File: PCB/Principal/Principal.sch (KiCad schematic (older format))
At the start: 17 parts, among them J1 STM32_P1, J2 STM32_P2, J3 Sensor_Golpes, J4 Teclado, J5 Sensor_Unidades, J6 Display_16x2, J7 Lector_RFID, J8 IN_Alimentación, SW1 SW_Power

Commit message: Alta plaquita guacho
Hay que acomodarla pero no quedo ningun puente.
Cambie TODOS los GPIO. Atento.
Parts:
- removed SW1: SW_Power, symbol Switch:SW_DPST
- added RV1: Display_Brillo, Potentiometers:Potentiometer_Trimmer_Bourns_3266Y, symbol Device:R_POT_TRIM_US
- D1: footprint (none) -> LEDs:LED_D5.0mm
- J1, J2: footprint Pin_Headers:Pin_Header_Straight_2x25_Pitch2.00mm -> Pin_Headers:Pin_Header_Straight_2x25_Pitch2.54mm
- J3, J5, J7: footprint (none) -> Connectors_Terminal_Blocks:TerminalBlock_bornier-3_P5.08mm
- J4: footprint (none) -> Pin_Headers:Pin_Header_Straight_1x08_Pitch2.54mm
- J6: footprint (none) -> Pin_Headers:Pin_Header_Straight_1x16_Pitch2.54mm
- J8: footprint (none) -> Connectors_Terminal_Blocks:TerminalBlock_bornier-2_P5.08mm
- R1, R2, R3, R4, R5, R6, R7: footprint (none) -> Resistors_THT:R_Axial_DIN0207_L6.3mm_D2.5mm_P10.16mm_Horizontal
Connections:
- wire segments 71 -> 104
- no-connect marks 0 -> 90
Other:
- moved on the sheet: D1, J3, J4, J5, J6, J7, J8, R1, R2, R3, R4, R5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

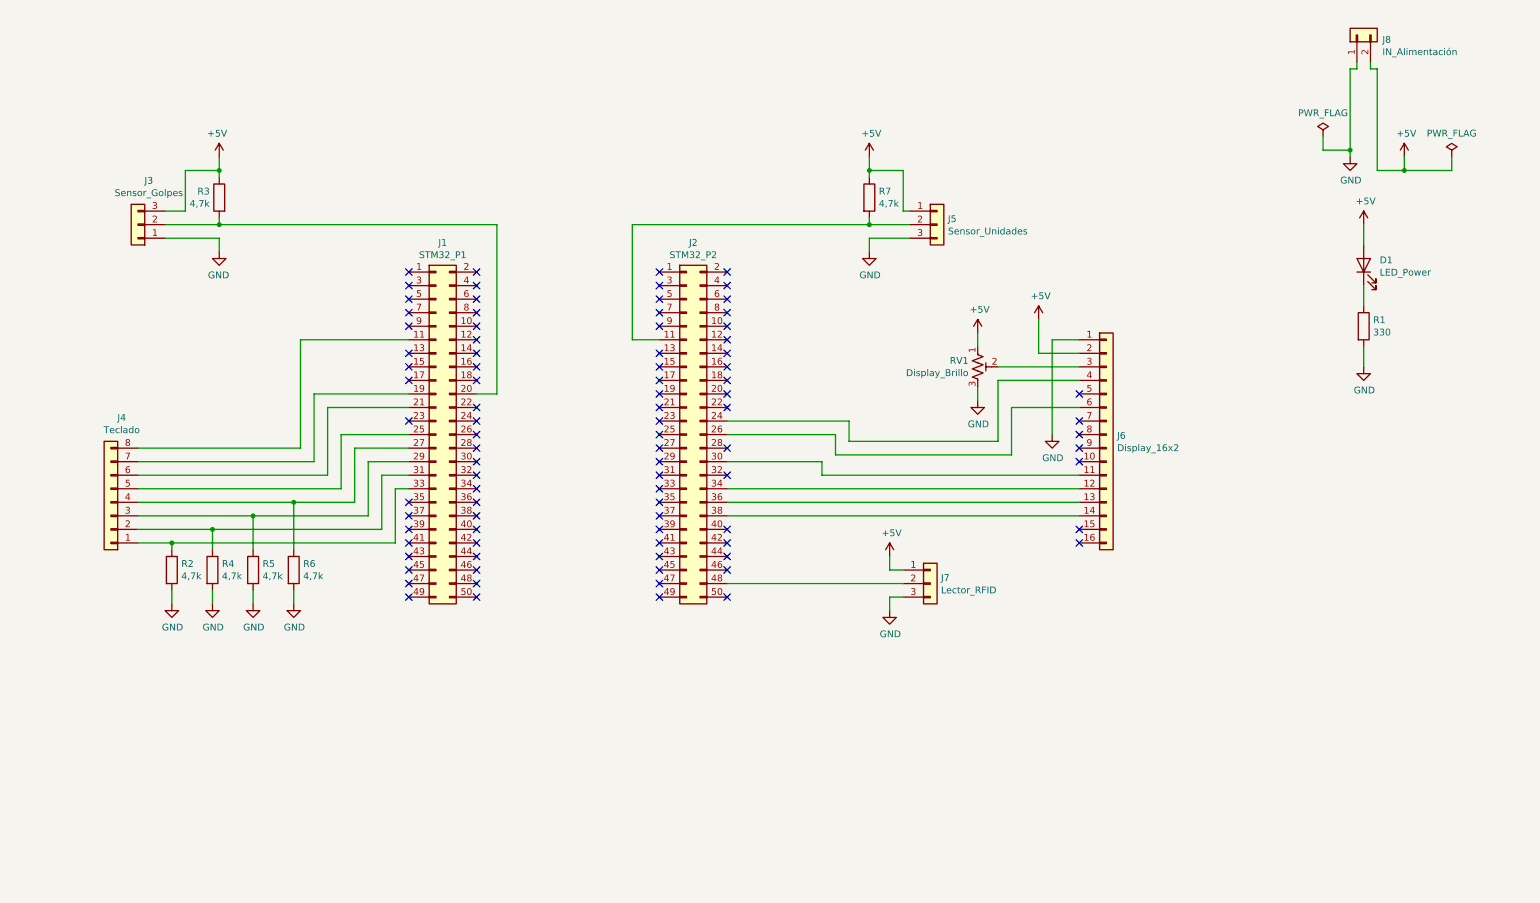
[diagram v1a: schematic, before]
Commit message: Sumando cambios al PCB
Se agrego al esquematico fuente de 5V con 7805 y la conexion del rfid.
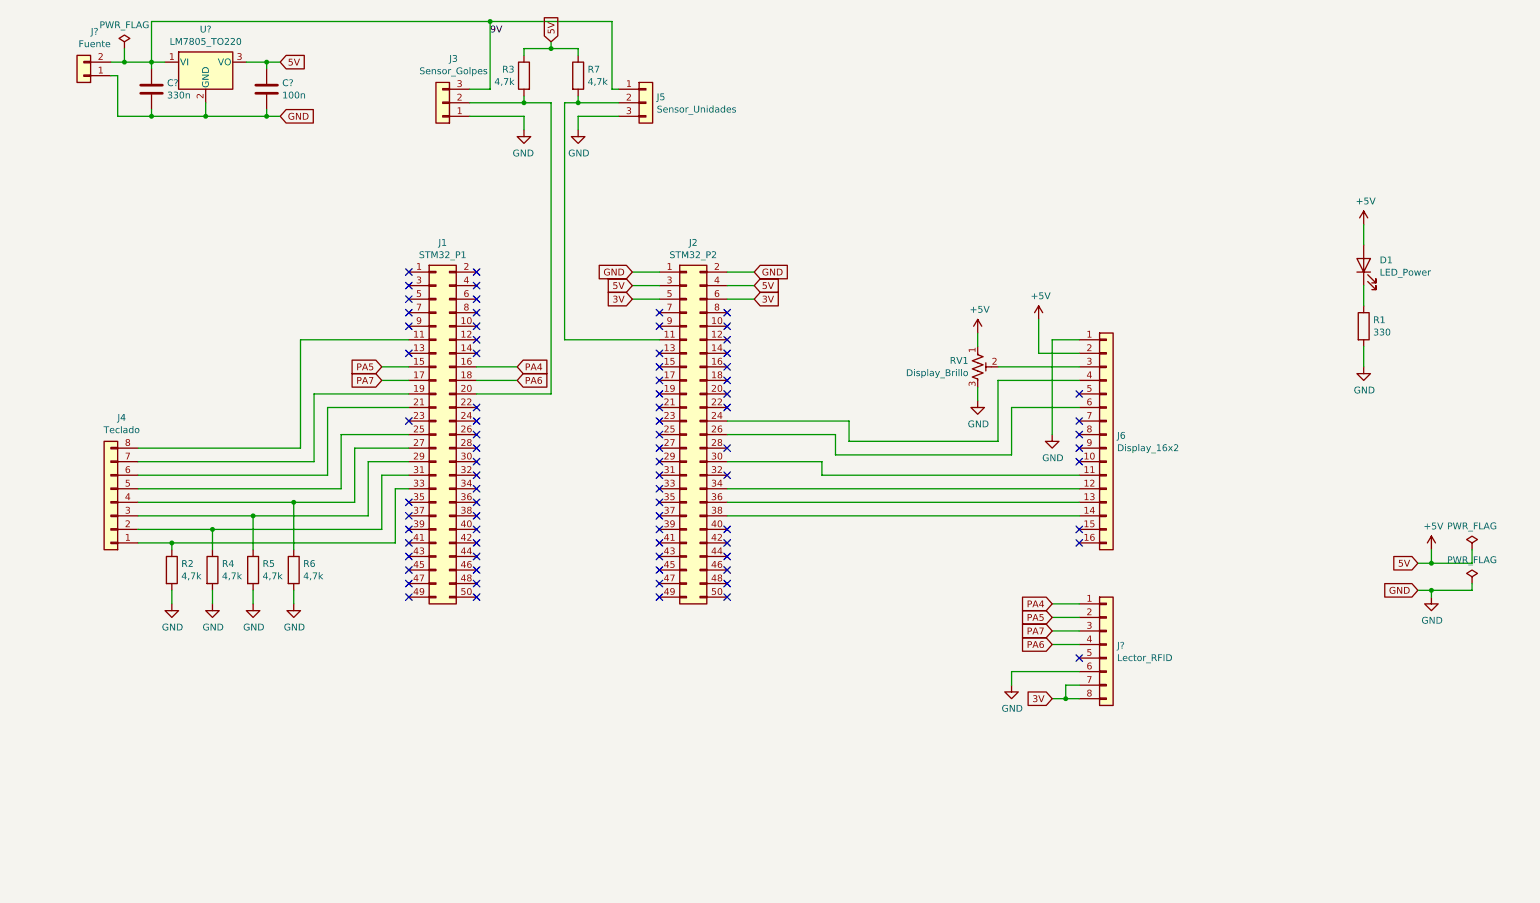
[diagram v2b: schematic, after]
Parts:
- removed J7: Lector_RFID, Connectors_Terminal_Blocks:TerminalBlock_bornier-3_P5.08mm, symbol Connector_Generic:Conn_01x03
- removed J8: IN_Alimentación, Connectors_Terminal_Blocks:TerminalBlock_bornier-2_P5.08mm, symbol Connector_Generic:Conn_01x02
- added C?: 330n, symbol Device:C
- added C?: 100n, symbol Device:C
- added J?: Fuente, symbol Connector_Generic:Conn_01x02
- added J?: Lector_RFID, symbol Connector_Generic:Conn_01x08
- added U?: LM7805_TO220, Package_TO_SOT_THT:TO-220-3_Vertical, symbol Regulator_Linear:LM7805_TO220
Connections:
- net +5V: now also J2.3 (Pin_3), J2.4 (Pin_4), C?.1, U?.3 (VO); no longer J3.3 (Pin_3), J5.1 (Pin_1)
- net GND: now also J2.1 (Pin_1), J2.2 (Pin_2), C?.2, C?.2, J?.1 (Pin_1), J?.6 (Pin_6), U?.2 (GND)
- net PA5: now reaches J1.15 (Pin_15)
- net PA5: now also J?.2 (Pin_2)
- net PA4: now reaches J1.16 (Pin_16)
- net PA4: now also J?.1 (Pin_1)
- net PA7: now reaches J1.17 (Pin_17)
- net PA7: now also J?.3 (Pin_3)
- net PA6: now reaches J1.18 (Pin_18)
- net PA6: now also J?.4 (Pin_4)
- net 3V: now reaches J2.5 (Pin_5)
- net 3V: now also J2.6 (Pin_6), J?.7 (Pin_7), J?.8 (Pin_8)
- new net 9V: C?.1, J3.3 (Pin_3), J5.1 (Pin_1), J?.2 (Pin_2), U?.1 (VI)
- no-connect marks 90 -> 82
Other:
- moved on the sheet: J3, J5, R3, R7

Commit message: Fin esquematico.
Ahora falta PCB
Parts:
- removed J4: Teclado, Pin_Headers:Pin_Header_Straight_1x08_Pitch2.54mm, symbol Connector_Generic:Conn_01x08
- removed J6: Display_16x2, Pin_Headers:Pin_Header_Straight_1x16_Pitch2.54mm, symbol Connector_Generic:Conn_01x16
- removed J?: Lector_RFID, symbol Connector_Generic:Conn_01x08
- added J6, J8: Conn_02x08_Counter_Clockwise, Pin_Headers:Pin_Header_Straight_2x08_Pitch2.54mm, symbol Connector_Generic:Conn_02x08_Counter_Clockwise
- added J7: Conn_02x20_Counter_Clockwise, Pin_Headers:Pin_Header_Straight_2x20_Pitch2.54mm, symbol Connector_Generic:Conn_02x20_Counter_Clockwise
- added J9: Jack-DC, Connectors:BARREL_JACK, symbol Connector:Jack-DC
- C1, C2: renamed from C?; footprint (none) -> Capacitors_THT:C_Disc_D7.5mm_W2.5mm_P5.00mm
- J4: renamed from J?; footprint (none) -> Connectors_Terminal_Blocks:TerminalBlock_bornier-2_P5.08mm
- R1: value 330 -> 680
- gave numbers to parts that had none: 1
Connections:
- net +5V: now also J7.2 (Pin_2), J7.39 (Pin_39); no longer D1.2 (A)
- net 3V: now also J8.10 (Pin_10), J8.7 (Pin_7), J8.8 (Pin_8), J8.9 (Pin_9)
- net 9V: now also D1.2 (A), J9.1
- net GND: now also J7.1 (Pin_1), J7.40 (Pin_40), J8.11 (Pin_11), J8.6 (Pin_6), J9.2
- net PA4: now also J8.1 (Pin_1), J8.16 (Pin_16)
- net PA5: now also J8.15 (Pin_15), J8.2 (Pin_2)
- net PA6: now also J8.13 (Pin_13), J8.4 (Pin_4)
- net PA7: now also J8.14 (Pin_14), J8.3 (Pin_3)
- net at J1.11 (Pin_11): now also J6.8 (Pin_8), J6.9 (Pin_9)
- net at J1.19 (Pin_19): now also J6.10 (Pin_10), J6.7 (Pin_7)
- net at J1.21 (Pin_21): now also J6.11 (Pin_11), J6.6 (Pin_6)
- net at J1.25 (Pin_25): now also J6.12 (Pin_12), J6.5 (Pin_5)
- net at J1.27 (Pin_27), R6.1: now also J6.13 (Pin_13), J6.4 (Pin_4)
- net at J1.29 (Pin_29), R5.1: now also J6.14 (Pin_14), J6.3 (Pin_3)
- net at J1.31 (Pin_31), R4.1: now also J6.15 (Pin_15), J6.2 (Pin_2)
- net at J1.33 (Pin_33), R2.1: now also J6.1 (Pin_1), J6.16 (Pin_16)
- net at J2.24 (Pin_24): now also J7.37 (Pin_37), J7.4 (Pin_4)
- net at J2.26 (Pin_26): now also J7.35 (Pin_35), J7.6 (Pin_6)
- net at J2.30 (Pin_30): now also J7.11 (Pin_11), J7.30 (Pin_30)
- net at J2.34 (Pin_34): now also J7.12 (Pin_12), J7.29 (Pin_29)
- net at J2.36 (Pin_36): now also J7.13 (Pin_13), J7.28 (Pin_28)
- net at J2.38 (Pin_38): now also J7.14 (Pin_14), J7.27 (Pin_27)
- net at RV1.2: now also J7.3 (Pin_3), J7.38 (Pin_38)
- no-connect marks 82 -> 98
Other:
- moved on the sheet: D1, R1

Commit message: Fin PCB re piola
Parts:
- removed J6, J8: Conn_02x08_Counter_Clockwise, Pin_Headers:Pin_Header_Straight_2x08_Pitch2.54mm, symbol Connector_Generic:Conn_02x08_Counter_Clockwise
- removed J7: Conn_02x20_Counter_Clockwise, Pin_Headers:Pin_Header_Straight_2x20_Pitch2.54mm, symbol Connector_Generic:Conn_02x20_Counter_Clockwise
- added J6: Conn_Teclado, Connector_PinSocket_2.54mm:PinSocket_2x08_P2.54mm_Vertical, symbol Connector_Generic:Conn_02x08_Odd_Even
- added J7: Conn_Display, Connector_PinSocket_2.54mm:PinSocket_2x20_P2.54mm_Vertical, symbol Connector_Generic:Conn_02x20_Odd_Even
- added J8: Conn_RFID, Connector_PinSocket_2.54mm:PinSocket_2x08_P2.54mm_Vertical, symbol Connector_Generic:Conn_02x08_Odd_Even
- added R10, R11, R8, R9: 4,7k, Resistor_THT:R_Axial_DIN0207_L6.3mm_D2.5mm_P10.16mm_Horizontal, symbol Device:R
- added SW1: InputPullUp1, TerminalBlock:TerminalBlock_bornier-2_P5.08mm, symbol Switch:SW_SPST
- added SW2: InputPullUp2, TerminalBlock:TerminalBlock_bornier-2_P5.08mm, symbol Switch:SW_SPST
- added SW3: InputPullUp3, TerminalBlock:TerminalBlock_bornier-2_P5.08mm, symbol Switch:SW_SPST
- added SW4: InputPullUp4, TerminalBlock:TerminalBlock_bornier-2_P5.08mm, symbol Switch:SW_SPST
- C1, C2: footprint Capacitors_THT:C_Disc_D7.5mm_W2.5mm_P5.00mm -> Capacitor_THT:C_Disc_D7.5mm_W2.5mm_P5.00mm
- D1: footprint LEDs:LED_D5.0mm -> LED_THT:LED_D5.0mm
- J1, J2: footprint Pin_Headers:Pin_Header_Straight_2x25_Pitch2.54mm -> Connector_PinHeader_2.54mm:PinHeader_2x25_P2.54mm_Vertical
- J3, J5: footprint Connectors_Terminal_Blocks:TerminalBlock_bornier-3_P5.08mm -> TerminalBlock:TerminalBlock_bornier-3_P5.08mm
- J4: footprint Connectors_Terminal_Blocks:TerminalBlock_bornier-2_P5.08mm -> TerminalBlock:TerminalBlock_bornier-2_P5.08mm
- J9: footprint Connectors:BARREL_JACK -> Connector_BarrelJack:BarrelJack_Horizontal
- R1, R2, R3, R4, R5, R6, R7: footprint Resistors_THT:R_Axial_DIN0207_L6.3mm_D2.5mm_P10.16mm_Horizontal -> Resistor_THT:R_Axial_DIN0207_L6.3mm_D2.5mm_P10.16mm_Horizontal
- RV1: footprint Potentiometers:Potentiometer_Trimmer_Bourns_3266Y -> Potentiometer_THT:Potentiometer_Bourns_3266Y_Vertical
- U1: value LM7805_TO220 -> LM7805
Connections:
- net +5V: now also J7.3 (Pin_3), J7.4 (Pin_4), R10.1, R11.1, R8.1, R9.1
- net 3V: now also J8.13 (Pin_13), J8.14 (Pin_14), J8.15 (Pin_15), J8.16 (Pin_16)
- net GND: now also J7.1 (Pin_1), J7.2 (Pin_2), J8.11 (Pin_11), J8.12 (Pin_12), SW1.2 (B), SW2.2 (B), SW3.2 (B), SW4.2 (B)
- net PA4: now also J8.1 (Pin_1), J8.2 (Pin_2)
- net PA5: now also J8.3 (Pin_3), J8.4 (Pin_4)
- net PA6: now also J8.7 (Pin_7), J8.8 (Pin_8)
- net PA7: now also J8.5 (Pin_5), J8.6 (Pin_6)
- net at J1.11 (Pin_11): now also J6.15 (Pin_15), J6.16 (Pin_16)
- net at J1.19 (Pin_19): now also J6.13 (Pin_13), J6.14 (Pin_14)
- net at J1.21 (Pin_21): now also J6.11 (Pin_11), J6.12 (Pin_12)
- net at J1.25 (Pin_25): now also J6.10 (Pin_10), J6.9 (Pin_9)
- net at J1.27 (Pin_27), R6.1: now also J6.7 (Pin_7), J6.8 (Pin_8)
- net at J1.29 (Pin_29), R5.1: now also J6.5 (Pin_5), J6.6 (Pin_6)
- net at J1.31 (Pin_31), R4.1: now also J6.3 (Pin_3), J6.4 (Pin_4)
- net at J1.33 (Pin_33), R2.1: now also J6.1 (Pin_1), J6.2 (Pin_2)
- net at J1.37 (Pin_37): now also R11.2, SW4.1 (A)
- net at J1.39 (Pin_39): now also R10.2, SW3.1 (A)
- net at J1.41 (Pin_41): now also R9.2, SW2.1 (A)
- net at J1.43 (Pin_43): now also R8.2, SW1.1 (A)
- net at J2.24 (Pin_24): now also J7.7 (Pin_7), J7.8 (Pin_8)
- net at J2.26 (Pin_26): now also J7.11 (Pin_11), J7.12 (Pin_12)
- net at J2.30 (Pin_30): now also J7.21 (Pin_21), J7.22 (Pin_22)
- net at J2.34 (Pin_34): now also J7.23 (Pin_23), J7.24 (Pin_24)
- net at J2.36 (Pin_36): now also J7.25 (Pin_25), J7.26 (Pin_26)
- net at J2.38 (Pin_38): now also J7.27 (Pin_27), J7.28 (Pin_28)
- net at RV1.2: now also J7.5 (Pin_5), J7.6 (Pin_6)
- no-connect marks 98 -> 94
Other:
- moved on the sheet: R2, R4, R5, R6
